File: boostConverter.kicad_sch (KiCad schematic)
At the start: 12 parts, among them Q1 PMV37ENEAR

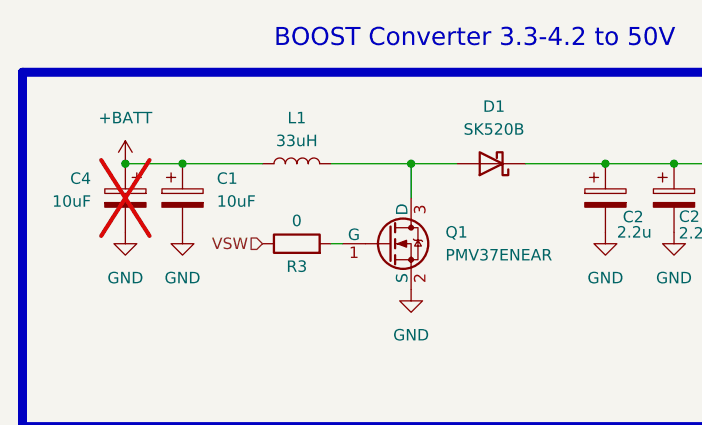
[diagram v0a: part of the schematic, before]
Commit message: version 2 with 0.8mm thickness
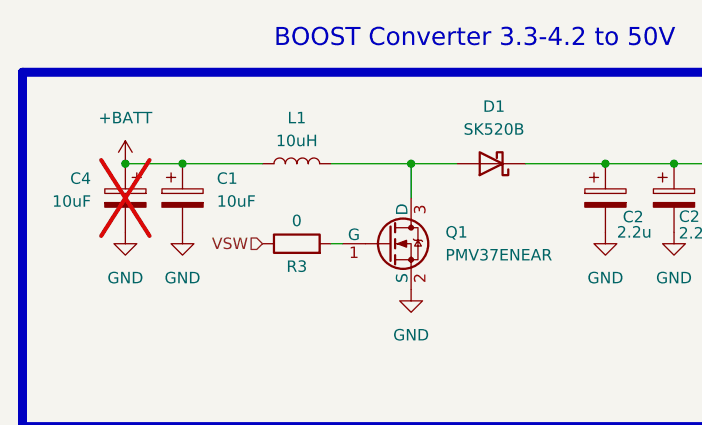
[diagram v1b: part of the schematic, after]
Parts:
- L1: value 33uH -> 10uH; footprint Library:IND_104CDM_SUM -> Library:INDPM7366X300N; Detailed Description 33 µH Shielded Molded Inductor 4.1 A 92mOhm Max Nonstandard -> 10 µH Shielded Inductor 4 A 68mOhm Max Nonstandard; Manufacturer Sumida America Components Inc. -> KYOCERA AVX; Manufacturer Part Number 104CDMCCDS-330MC -> LMLP07A7M100DTAS; Package TH -> SMD
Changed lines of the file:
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@@
       (effects (font (size 1.27 1.27)))
     )
-    (property "Value" "33uH" (at 83.82 50.8 90)
+    (property "Value" "10uH" (at 83.82 50.8 90)
       (effects (font (size 1.27 1.27)))
     )
-    (property "Footprint" "Library:IND_104CDM_SUM" (at 83.82 53.34 0)
+    (property "Footprint" "Library:INDPM7366X300N" (at 83.82 53.34 0)
       (effects (font (size 1.27 1.27)) hide)
     )
@@
       (effects (font (size 1.27 1.27)) hide)
     )
-    (property "Manufacturer" "Sumida America Components Inc." (at 83.82 53.34 90)
+    (property "Manufacturer" "KYOCERA AVX" (at 83.82 53.34 90)
       (effects (font (size 1.27 1.27)) hide)
     )
-    (property "Manufacturer Part Number" "104CDMCCDS-330MC" (at 83.82 53.34 90)
+    (property "Manufacturer Part Number" "LMLP07A7M100DTAS" (at 83.82 53.34 90)
       (effects (font (size 1.27 1.27)) hide)
     )
-    (property "Description" "FIXED IND 33UH 4.1A 92 MOHM SMD" (at 83.82 53.34 90)
+    (property "Description" "FIXED IND 10UH 4A 68 MOHM SMD" (at 83.82 53.34 90)
       (effects (font (size 1.27 1.27)) hide)
     )
-    (property "Detailed Description" "33 µH Shielded Molded Inductor 4.1 A 92mOhm Max Nonstandard" (at 83.82 53.34 90)
+    (property "Detailed Description" "10 µH Shielded Inductor 4 A 68mOhm Max Nonstandard" (at 83.82 53.34 90)
       (effects (font (size 1.27 1.27)) hide)
     )
-    (property "Package" "TH" (at 83.82 53.34 90)
+    (property "Package" "SMD" (at 83.82 53.34 90)
       (effects (font (size 1.27 1.27)) hide)
     )

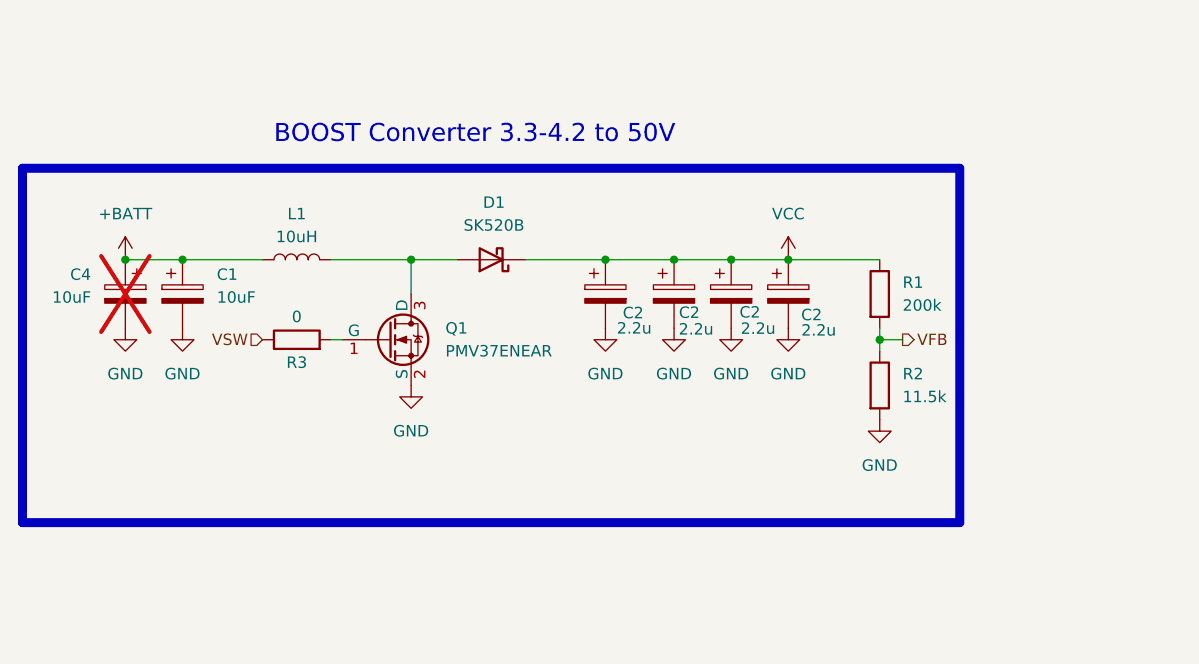
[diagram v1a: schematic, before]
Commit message: v3: removed digital potentiometer, added 8 discrete resistors and one GPIO expander
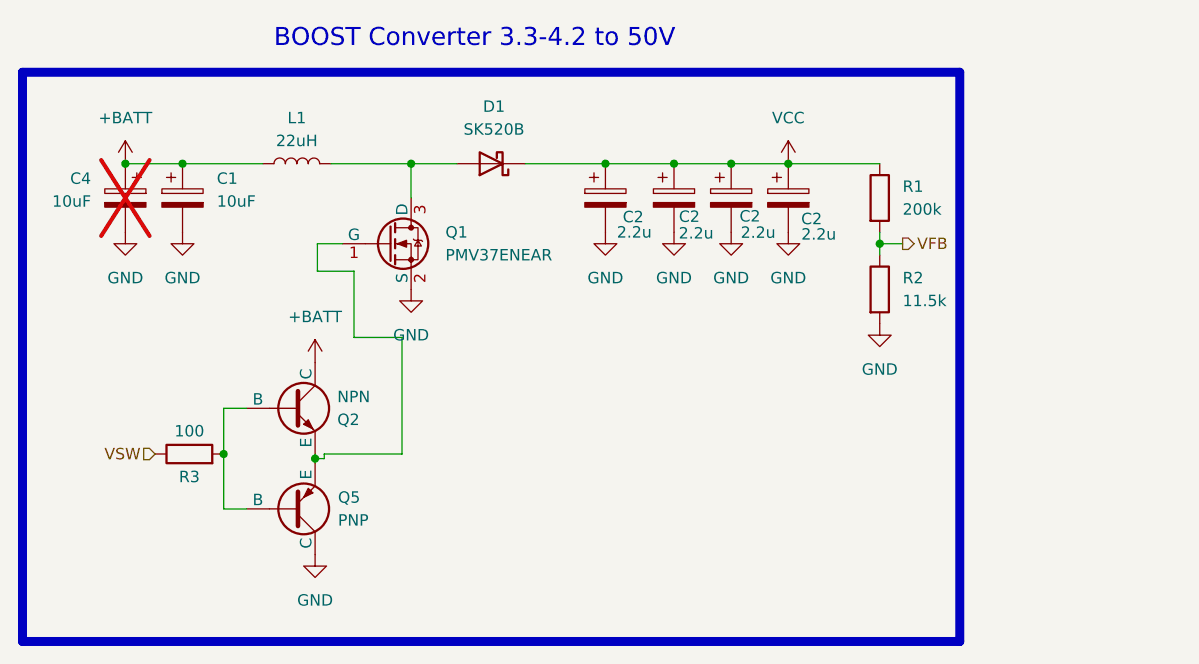
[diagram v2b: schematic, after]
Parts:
- added Q2: NPN, Package_TO_SOT_SMD:SOT-23, symbol Simulation_SPICE:NPN
- added Q5: PNP, Package_TO_SOT_SMD:SOT-23, symbol Simulation_SPICE:PNP
- L1: value 10uH -> 22uH; Detailed Description 10 µH Shielded Inductor 4 A 68mOhm Max Nonstandard -> 22 µH Shielded Drum Core, Wirewound Inductor 3.4 A 168mOhm 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; Manufacturer KYOCERA AVX -> Bourns Inc.; Manufacturer Part Number LMLP07A7M100DTAS -> SRP6030VA-220M
- R3: value 0 -> 100; Long Description 0 Ohms Jumper Chip Resistor 0402 (1005 Metric) Moisture Res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 -> 100 Ohms Jumper Chip Resistor 0402 (1005 Metric) Moisture R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; Manufacturer Part Number RC0402FR-070RL -> RC0402FR-07100RL
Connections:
- net +BATT: now also Q2.3 (C)
- net GND: now also Q5.3 (C)
- net at R3.2: now also Q2.1 (B), Q5.1 (B); no longer Q1.1 (G)
- new net: Q1.1 (G), Q2.2 (E), Q5.2 (E)
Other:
- moved on the sheet: C1, C2, C4, D1, L1, Q1, R1, R2

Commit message: version 4: changed GPIO expander, added current sense resistor to electrodes, added buzzer pins, fixed some gpio inputs that needs to be pulled high, added battery charge detection, added battery level measurement feature
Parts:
- C1, C4: Long Description (none) -> 10 µF ±10% 16V Ceramic Capacitor X7R 0805 (2012 Metric)
- L1: Long Description (none) -> 22 µH Shielded Drum Core, Wirewound Inductor 3.4 A 168mOhm 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
- Q1: Long Description (none) -> N-Channel 60 V 3.5A (Ta) 710mW (Ta), 8.3W (Tc) Surface Moun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
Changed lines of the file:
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@@
+      (effects (font (size 1.27 1.27)) hide)
+    )
+    (property "Description" "CAP CER 10UF 16V X7R 0805" (at 71.12 46.482 0)
+      (effects (font (size 1.27 1.27)) hide)
+    )
+    (property "Long Description" "10 µF ±10% 16V Ceramic Capacitor X7R 0805 (2012 Metric)" (at 71.12 46.482 0)
       (effects (font (size 1.27 1.27)) hide)
     )
@@
       (effects (font (size 1.27 1.27)) hide)
     )
+    (property "Description" "MOSFET N-CH 60V 3.5A TO236AB" (at 93.98 51.562 0)
+      (effects (font (size 1.27 1.27)) hide)
+    )
+    (property "Long Description" "N-Channel 60 V 3.5A (Ta) 710mW (Ta), 8.3W (Tc) Surface Mount TO-236AB" (at 93.98 51.562 0)
+      (effects (font (size 1.27 1.27)) hide)
+    )
     (pin "1")
     (pin "2")
@@
       (effects (font (size 1.27 1.27)) hide)
     )
+    (property "Long Description" "22 µH Shielded Drum Core, Wirewound Inductor 3.4 A 168mOhm Max Nonstandard" (at 83.82 42.672 0)
+      (effects (font (size 1.27 1.27)) hide)
+    )
     (pin "1")
     (pin "2")
@@
       (effects (font (size 1.27 1.27)) hide)
     )
+    (property "Description" "CAP CER 10UF 16V X7R 0805" (at 64.77 46.482 0)
+      (effects (font (size 1.27 1.27)) hide)
+    )
+    (property "Long Description" "10 µF ±10% 16V Ceramic Capacitor X7R 0805 (2012 Metric)" (at 64.77 46.482 0)
+      (effects (font (size 1.27 1.27)) hide)
+    )

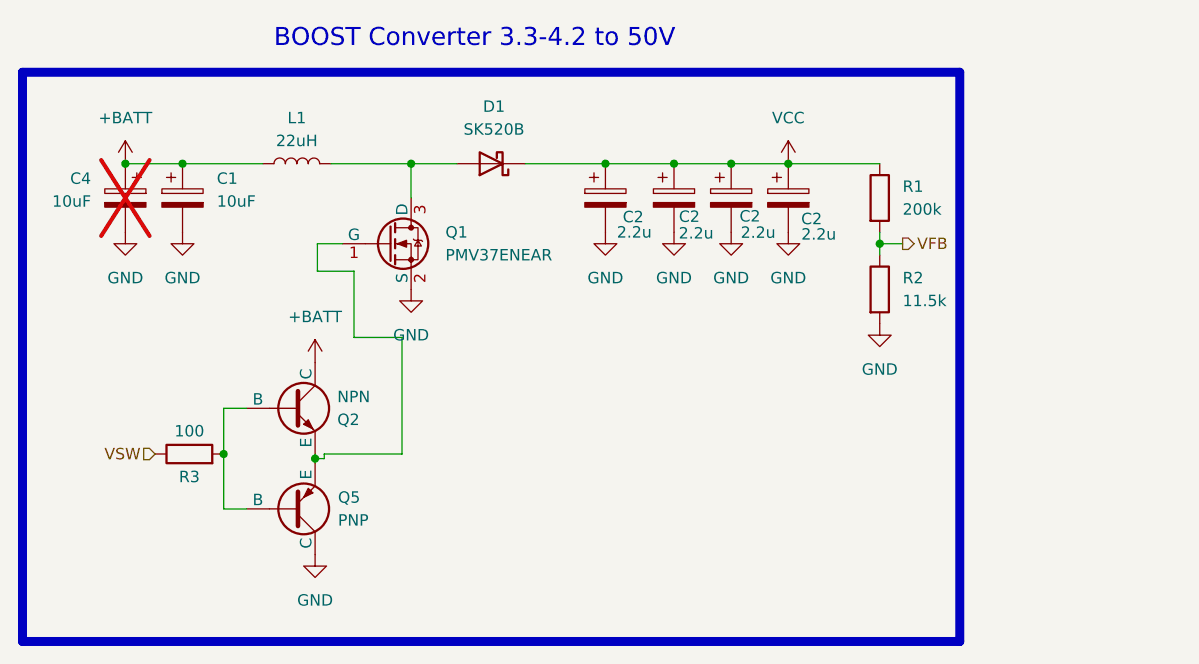
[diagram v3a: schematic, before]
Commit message: version 5: replaced ESP32-WROVER module with ESP-Mini, removed 2.5mm plugs, changed USB connector and routed electrode signals on it, added RC snubber circuit to boost converter and output caps to reduce switching loop
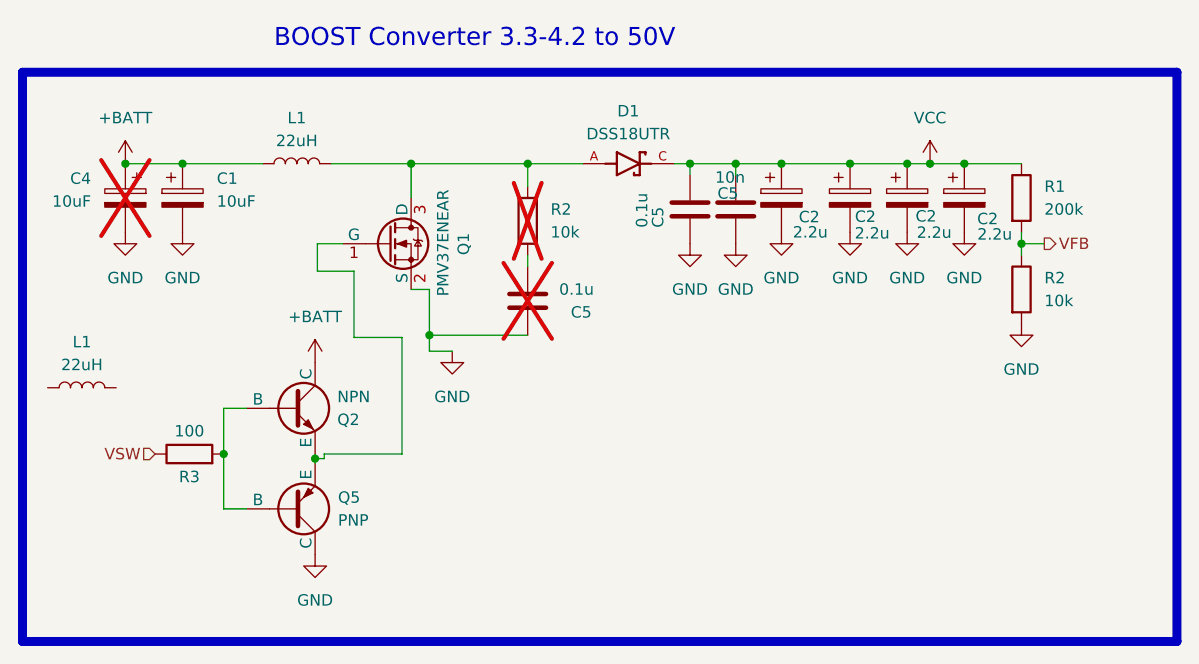
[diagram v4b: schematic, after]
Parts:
- removed D1: SK520B, Diode_SMD:D_SMB, symbol Device:D_Schottky
- added C5: 0.1u, Capacitor_SMD:C_0402_1005Metric, symbol Device:C
- added C5: 10n, Capacitor_SMD:C_0603_1608Metric, symbol Device:C
- added C5: 0.1u, Capacitor_SMD:C_0603_1608Metric, symbol Device:C
- added D1: DSS18UTR, Library:SODFL3618X110N, symbol 2023-09-03_14-36-57:DSS18UTR
- added L1: 22uH, Library:IND_AMDLA1004S-330MT, symbol Device:L
- added R2: 10k, Resistor_SMD:R_0402_1005Metric, symbol Device:R
- Q2: Long Description Bipolar (BJT) Transistor NPN 60 V 2 A 100MHz 460 mW Surface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 -> Bipolar (BJT) Transistor NPN 60 V 1 A 150MHz 460 mW Surface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; Manufacturer On Semiconductor -> Diodes Incorporated; Manufacturer Part Number NSS60201LT1G -> DNBT8105-7
- R2: value 11.5k -> 10k; Long Description 11.5 kOhms ±1% 0.063W, 1/16W Chip Resistor 0402 (1005 Metri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 -> 10 kOhms ±1% 0.063W, 1/16W Chip Resistor 0402 (1005 Metric)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; Manufacturer Part Number RC0402FR-0711K5L -> RC0402FR-0710KL
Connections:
- net GND: now also C5.1, C5.2, C5.2
- net VCC: now also C5.1, C5.1, D1.C
- net at L1.2, Q1.3 (D): now also D1.A, R2.1
- new net: C5.2, R2.2
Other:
- moved on the sheet: C2, R1, R2

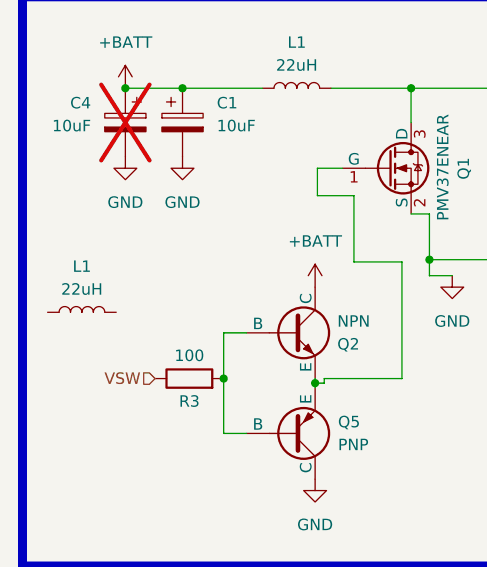
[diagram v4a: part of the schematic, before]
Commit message: Fixed electrode detection mechanism, modified position of USB Type-C port
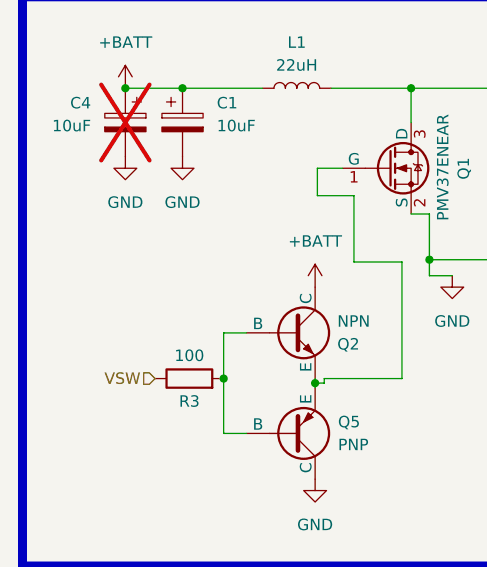
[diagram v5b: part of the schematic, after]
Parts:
- removed L1: 22uH, Library:IND_AMDLA1004S-330MT, symbol Device:L
- C5: Long Description 0.1 µF ±10% 100V Ceramic Capacitor X7R 0603 (1608 Metric) -> 10nF ±10% 100V Ceramic Capacitor X7R 0603 (1608 Metric)
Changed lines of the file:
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@@
       (effects (font (size 1.27 1.27)) hide)
     )
-    (property "Description" "0.1 µF ±10% 100V Ceramic Capacitor X7R 0603 (1608 Metric)" (at 132.588 47.752 0)
-      (effects (font (size 1.27 1.27)) hide)
-    )
-    (property "Long Description" "0.1 µF ±10% 100V Ceramic Capacitor X7R 0603 (1608 Metric)" (at 132.588 47.752 0)
+    (property "Description" "10nF ±10% 100V Ceramic Capacitor X7R 0603 (1608 Metric)" (at 132.588 47.752 0)
+      (effects (font (size 1.27 1.27)) hide)
+    )
+    (property "Long Description" "10nF ±10% 100V Ceramic Capacitor X7R 0603 (1608 Metric)" (at 132.588 47.752 0)
       (effects (font (size 1.27 1.27)) hide)
     )
@@
         )
       )
-    )
-  )
-  (symbol (lib_id "Device:L") (at 59.944 67.564 90) (unit 1)
-    (in_bom yes) (on_board yes) (dnp no) (fields_autoplaced)
-    (property "Reference" "L1" (at 59.944 62.484 90)
-      (effects (font (size 1.27 1.27)))
-    )
-    (property "Value" "22uH" (at 59.944 65.024 90)
-      (effects (font (size 1.27 1.27)))
-    )
-    (property "Footprint" "Library:IND_AMDLA1004S-330MT" (at 59.944 67.564 0)
-      (effects (font (size 1.27 1.27)) hide)
-    )
-    (property "Datasheet" "~" (at 59.944 67.564 0)
-      (effects (font (size 1.27 1.27)) hide)
-    )
-    (property "Manufacturer" "Bourns Inc." (at 59.944 67.564 90)
-      (effects (font (size 1.27 1.27)) hide)
-    )
-    (property "Manufacturer Part Number" "SRP6030VA-220M" (at 59.944 67.564 90)
-      (effects (font (size 1.27 1.27)) hide)
-    )
-    (property "Description" "FIXED IND 22UH 3.4A 168MOHM SMD" (at 59.944 67.564 90)
-      (effects (font (size 1.27 1.27)) hide)
-    )
-    (property "Detailed Description" "22 µH Shielded Drum Core, Wirewound Inductor 3.4 A 168mOhm Max Nonstandard" (at 59.944 67.564 90)
-      (effects (font (size 1.27 1.27)) hide)
-    )
-    (property "Package" "SMD" (at 59.944 67.564 90)
-      (effects (font (size 1.27 1.27)) hide)
-    )
-    (property "Long Description" "22 µH Shielded Drum Core, Wirewound Inductor 3.4 A 168mOhm Max Nonstandard" (at 59.944 67.564 0)
-      (effects (font (size 1.27 1.27)) hide)
-    )
-    (pin "1")
-    (pin "2")
-    (instances
-      (project "MaxTENS"
-        (path "/19b6afc4-eb08-418e-8b76-b08e19c3eaa1"
-          (reference "L1") (unit 1)
-        )
-        (path "/19b6afc4-eb08-418e-8b76-b08e19c3eaa1/82508d59-20f0-4a68-95de-e8096722e50d"
-          (reference "L2") (unit 1)
-        )
-      )
